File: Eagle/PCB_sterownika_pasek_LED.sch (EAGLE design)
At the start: 14 parts, among them IC3 NE555, Q1 IRF740

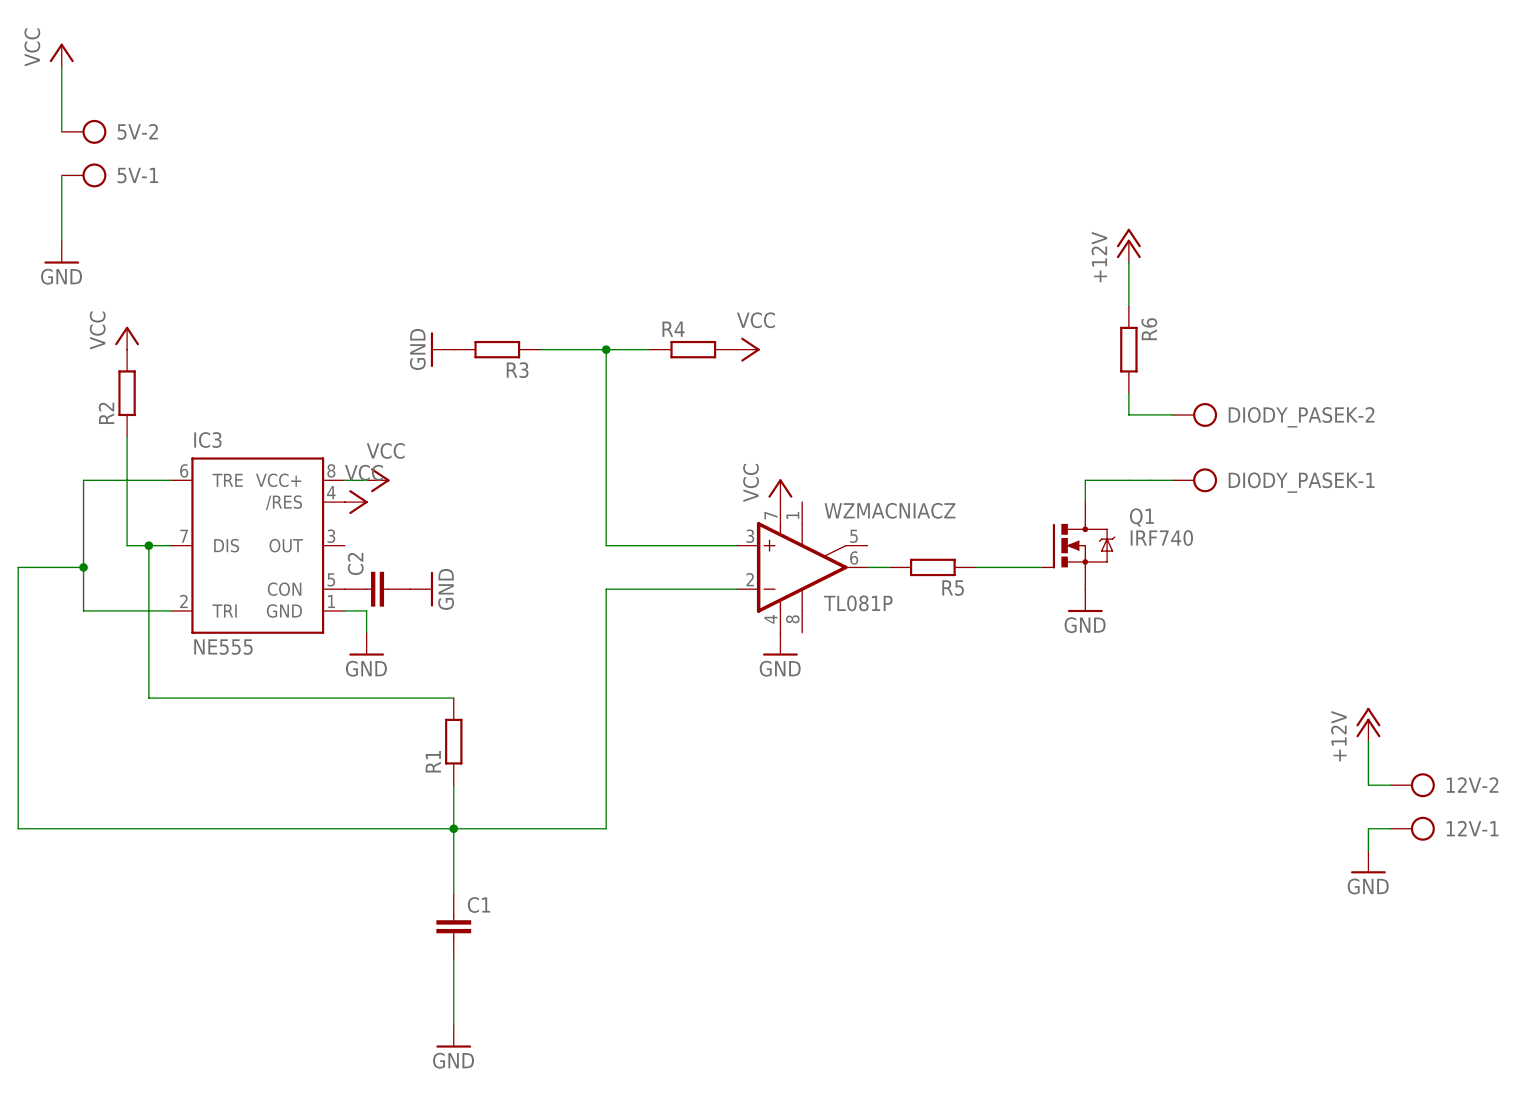
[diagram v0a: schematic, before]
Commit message: zakończenie cz. elektronicznej.
Podłączenie na płytce stykowym pierwszych czujników + zamknięcie części sterownika do paska LED.
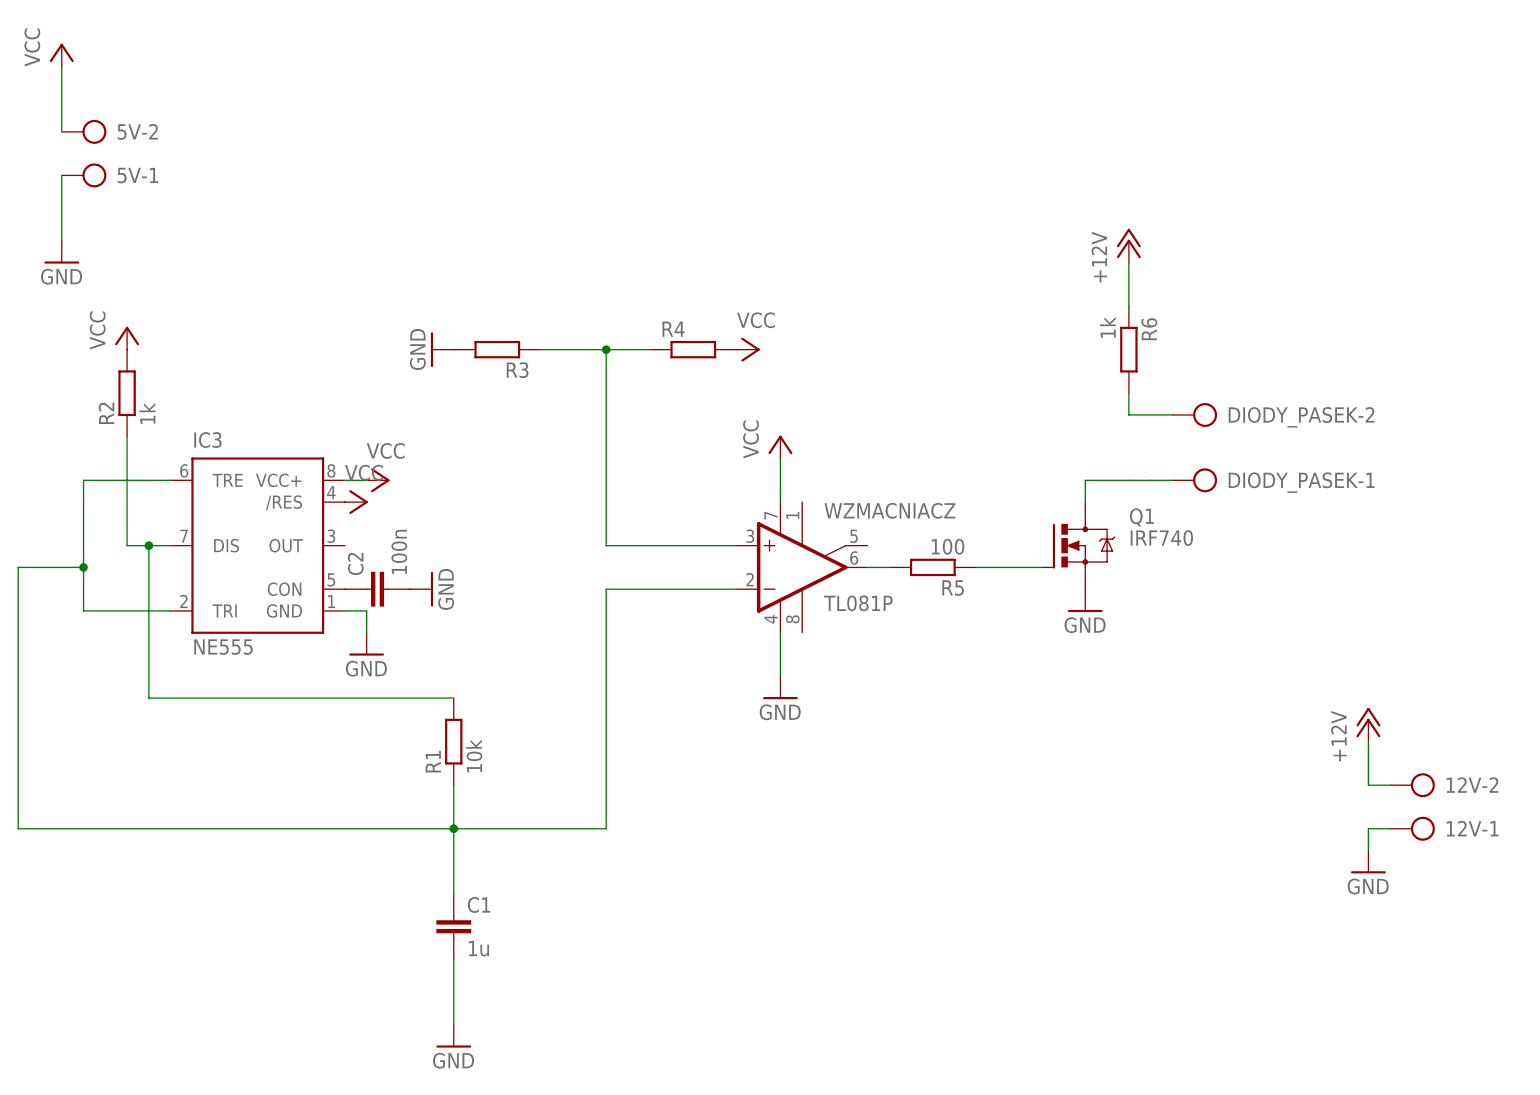
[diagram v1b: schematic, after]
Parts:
- C1: value (none) -> 1u
- C2: value (none) -> 100n
- R1: value (none) -> 10k
- R2, R6: value (none) -> 1k
- R5: value (none) -> 100
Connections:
- removed net N$3: WZMACNIACZ.-IN
- net N$5: now also WZMACNIACZ.-IN
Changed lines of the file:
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@@
 <part name="WZMACNIACZ" library="linear" deviceset="TL081" device="P"/>
 <part name="IC3" library="st-microelectronics" deviceset="NE555" device=""/>
-<part name="R2" library="eagle-ltspice" deviceset="R" device="0204/7"/>
+<part name="R2" library="eagle-ltspice" deviceset="R" device="0204/7" value="1k"/>
 <part name="R3" library="eagle-ltspice" deviceset="R" device="0204/7"/>
 <part name="GND1" library="supply1" deviceset="GND" device=""/>
 <part name="P+1" library="supply1" deviceset="VCC" device=""/>
 <part name="GND3" library="supply1" deviceset="GND" device=""/>
-<part name="C1" library="rcl" deviceset="C-EU" device="025-024X044"/>
+<part name="C1" library="rcl" deviceset="C-EU" device="025-024X044" value="1u"/>
 <part name="GND4" library="supply1" deviceset="GND" device=""/>
-<part name="R1" library="eagle-ltspice" deviceset="R" device="0204/7"/>
+<part name="R1" library="eagle-ltspice" deviceset="R" device="0204/7" value="10k"/>
 <part name="P+2" library="supply1" deviceset="VCC" device=""/>
 <part name="P+3" library="supply1" deviceset="VCC" device=""/>
-<part name="C2" library="rcl" deviceset="C-EU" device="025-024X044"/>
+<part name="C2" library="rcl" deviceset="C-EU" device="025-024X044" value="100n"/>
 <part name="GND2" library="supply1" deviceset="GND" device=""/>
 <part name="P+4" library="supply1" deviceset="VCC" device=""/>
@@
 <part name="P+6" library="supply1" deviceset="VCC" device=""/>
 <part name="GND6" library="supply1" deviceset="GND" device=""/>
-<part name="R5" library="eagle-ltspice" deviceset="R" device="0204/7"/>
+<part name="R5" library="eagle-ltspice" deviceset="R" device="0204/7" value="100"/>
 <part name="GND7" library="supply1" deviceset="GND" device=""/>
-<part name="R6" library="eagle-ltspice" deviceset="R" device="0204/7"/>
+<part name="R6" library="eagle-ltspice" deviceset="R" device="0204/7" value="1k"/>
 <part name="P+7" library="supply1" deviceset="+12V" device=""/>
 <part name="12V" library="con-ptr500" deviceset="AK500/2" device=""/>
@@
 <instance part="P+5" gate="VCC" x="86.36" y="96.52" rot="R270"/>
 <instance part="GND5" gate="1" x="48.26" y="96.52" rot="R270"/>
-<instance part="P+6" gate="VCC" x="88.9" y="81.28"/>
-<instance part="GND6" gate="1" x="88.9" y="60.96"/>
+<instance part="P+6" gate="VCC" x="88.9" y="86.36"/>
+<instance part="GND6" gate="1" x="88.9" y="55.88"/>
 <instance part="R5" gate="G$1" x="106.68" y="71.12" rot="R180"/>
 <instance part="GND7" gate="1" x="124.46" y="66.04"/>
@@
 </busses>
 <nets>
-<net name="N$3" class="0">
-<segment>
-<pinref part="WZMACNIACZ" gate="A" pin="-IN"/>
-<wire x1="83.82" y1="68.58" x2="68.58" y2="68.58" width="0.1524" layer="91"/>
-</segment>
-</net>
 <net name="N$1" class="0">
 <segment>
-<pinref part="WZMACNIACZ" gate="A" pin="+IN"/>
-<wire x1="83.82" y1="73.66" x2="68.58" y2="73.66" width="0.1524" layer="91"/>
 <wire x1="68.58" y1="73.66" x2="68.58" y2="96.52" width="0.1524" layer="91"/>
 <pinref part="R3" gate="G$1" pin="1"/>
@@
 <wire x1="68.58" y1="96.52" x2="73.66" y2="96.52" width="0.1524" layer="91"/>
 <junction x="68.58" y="96.52"/>
+<pinref part="WZMACNIACZ" gate="A" pin="+IN"/>
+<wire x1="83.82" y1="73.66" x2="68.58" y2="73.66" width="0.1524" layer="91"/>
 </segment>
 </net>
@@
 <pinref part="WZMACNIACZ" gate="A" pin="V-"/>
 <pinref part="GND6" gate="1" pin="GND"/>
+<wire x1="88.9" y1="58.42" x2="88.9" y2="63.5" width="0.1524" layer="91"/>
 </segment>
 <segment>
@@
 <pinref part="WZMACNIACZ" gate="A" pin="V+"/>
 <pinref part="P+6" gate="VCC" pin="VCC"/>
+<wire x1="88.9" y1="83.82" x2="88.9" y2="78.74" width="0.1524" layer="91"/>
 </segment>
 <segment>
@@
 <wire x1="50.8" y1="33.02" x2="50.8" y2="40.64" width="0.1524" layer="91"/>
 <pinref part="R1" gate="G$1" pin="1"/>
+<pinref part="WZMACNIACZ" gate="A" pin="-IN"/>
+<wire x1="68.58" y1="68.58" x2="83.82" y2="68.58" width="0.1524" layer="91"/>
 </segment>
 </net>
